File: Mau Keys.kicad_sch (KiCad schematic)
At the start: 2 parts

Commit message: holaaa
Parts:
- added NNV2: ~, symbol MCC NNV2:NNano_v2
- added Switch10, Switch11, Switch12, Switch13, Switch14, Switch15, Switch16, Switch17, Switch6, Switch7, Switch8, Switch9: ~, Switches:keyswitch_cherrymx_alps_choc12_slots_1u, symbol Switches:Kailh_ChocV2_Switch
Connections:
- net S1_P: now reaches Switch1.1
- net S1_P: now also Switch2.1
- net GND: now reaches Switch1.2
- net GND: now also Switch2.2
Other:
- moved on the sheet: Switch1

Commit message: Initial traces
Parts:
- added NNV2_R1: ~, Microcontroller:nice_nano, symbol MCC NNV2:NNano_v2
- added Switch3, Switch4, Switch5, SwitchR_1, SwitchR_10, SwitchR_11, SwitchR_12, SwitchR_13, SwitchR_14, SwitchR_15, SwitchR_16, SwitchR_17, SwitchR_2, SwitchR_3, SwitchR_4, SwitchR_5, SwitchR_6, SwitchR_7, SwitchR_8, SwitchR_9: ~, Switches:keyswitch_cherrymx_alps_choc12_slots_1u, symbol Switches:Kailh_ChocV2_Switch
- NNV2: footprint (none) -> Microcontroller:nice_nano
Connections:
- net GND: now also NNV2.1, NNV2.16, NNV2.4, NNV2.5, Switch10.2, Switch11.2, Switch12.2, Switch13.2, Switch14.2, Switch15.2, Switch16.2, Switch17.2, Switch6.2, Switch7.2, Switch8.2, Switch9.2, NNV2_R1.1, NNV2_R1.16, NNV2_R1.4, NNV2_R1.5, Switch3.2, Switch4.2, Switch5.2, SwitchR_1.2, SwitchR_10.2, SwitchR_11.2, SwitchR_12.2, SwitchR_13.2, SwitchR_14.2, SwitchR_15.2, SwitchR_16.2, SwitchR_17.2, SwitchR_2.2, SwitchR_3.2, SwitchR_4.2, SwitchR_5.2, SwitchR_6.2, SwitchR_7.2, SwitchR_8.2, SwitchR_9.2
- net S9: now reaches Switch9.1
- net S9: now also NNV2.26
- net S12: now reaches Switch12.1
- net S12: now also NNV2.7
- net S15: now reaches Switch15.1
- net S15: now also NNV2.11
- net S11: now reaches Switch11.1
- net S11: now also NNV2.6
- net S13: now reaches Switch13.1
- net S13: now also NNV2.8
- net S17: now reaches Switch17.1
- net S17: now also NNV2.13
- net S10: now reaches Switch10.1
- net S10: now also NNV2.2
- net S16: now reaches Switch16.1
- net S16: now also NNV2.12
- net S1: now reaches NNV2.10
- net S1: now also Switch1.1
- net VBAT: now reaches NNV2.14
- net VBAT: now also NNV2.15, NNV2_R1.14, NNV2_R1.15
- net RESET: now reaches NNV2.17
- net RESET: now also NNV2_R1.17
- net EXT_VCC: now reaches NNV2.18
- net EXT_VCC: now also NNV2_R1.18
- net S5: now reaches NNV2.19
- net S5: now also Switch5.1
- net S4: now reaches NNV2.20
- net S4: now also Switch4.1
- net S3: now reaches NNV2.21
- net S3: now also Switch3.1
- net S2: now reaches NNV2.22
- net S2: now also Switch2.1
- net S6: now reaches NNV2.23
- net S6: now also Switch6.1
- net S7: now reaches NNV2.24
- net S7: now also Switch7.1
- net S8: now reaches NNV2.25
- net S8: now also Switch8.1
- net S14: now reaches NNV2.9
- net S14: now also Switch14.1
- removed net S1_P: Switch1.1, Switch2.1
- new net S10_R: NNV2_R1.2, SwitchR_10.1
- new net S11_R: NNV2_R1.6, SwitchR_11.1
- new net S12_R: NNV2_R1.7, SwitchR_12.1
- new net S13_R: NNV2_R1.8, SwitchR_13.1
- new net S14_R: NNV2_R1.9, SwitchR_14.1
- new net S15_R: NNV2_R1.11, SwitchR_15.1
- new net S16_R: NNV2_R1.12, SwitchR_16.1
- new net S17_R: NNV2_R1.13, SwitchR_17.1
- new net S1_R: NNV2_R1.10, SwitchR_1.1
- new net S2_R: NNV2_R1.22, SwitchR_2.1
- new net S3_R: NNV2_R1.21, SwitchR_3.1
- new net S4_R: NNV2_R1.20, SwitchR_4.1
- new net S5_R: NNV2_R1.19, SwitchR_5.1
- new net S6_R: NNV2_R1.23, SwitchR_6.1
- new net S7_R: NNV2_R1.24, SwitchR_7.1
- new net S8_R: NNV2_R1.25, SwitchR_8.1
- new net S9_R: NNV2_R1.26, SwitchR_9.1
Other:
- moved on the sheet: Switch1

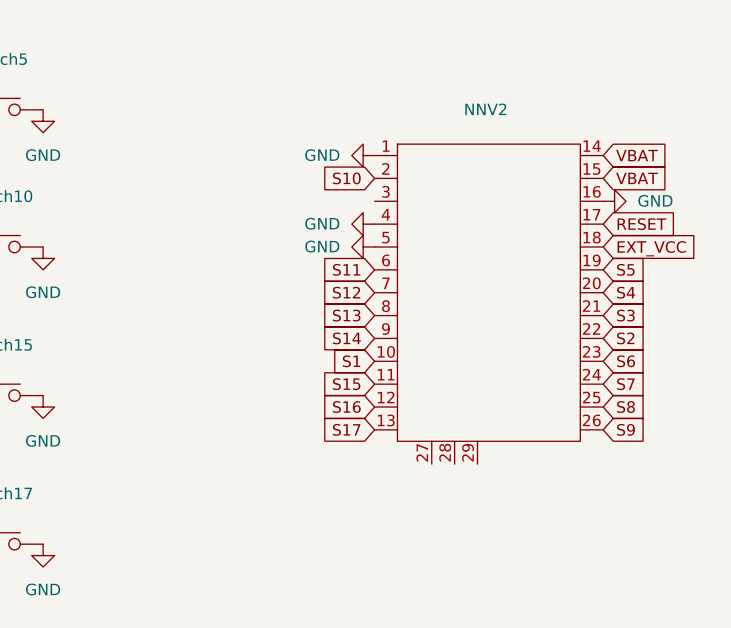
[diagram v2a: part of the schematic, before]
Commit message: Add traces upper left
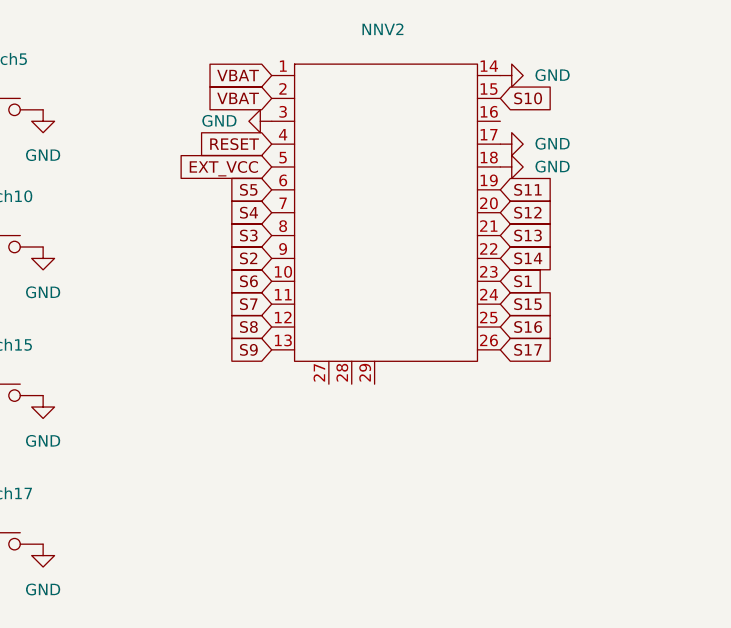
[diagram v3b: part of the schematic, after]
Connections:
- net EXT_VCC: now also NNV2.5; no longer NNV2.18
- net GND: now also NNV2.14, NNV2.17, NNV2.18, NNV2.3; no longer NNV2.1, NNV2.16, NNV2.4, NNV2.5
- net RESET: now also NNV2.4; no longer NNV2.17
- net S1: now also NNV2.23; no longer NNV2.10
- net S10: now also NNV2.15; no longer NNV2.2
- net S11: now also NNV2.19; no longer NNV2.6
- net S12: now also NNV2.20; no longer NNV2.7
- net S13: now also NNV2.21; no longer NNV2.8
- net S14: now also NNV2.22; no longer NNV2.9
- net S15: now also NNV2.24; no longer NNV2.11
- net S16: now also NNV2.25; no longer NNV2.12
- net S17: now also NNV2.26; no longer NNV2.13
- net S2: now also NNV2.9; no longer NNV2.22
- net S3: now also NNV2.8; no longer NNV2.21
- net S4: now also NNV2.7; no longer NNV2.20
- net S5: now also NNV2.6; no longer NNV2.19
- net S6: now also NNV2.10; no longer NNV2.23
- net S7: now also NNV2.11; no longer NNV2.24
- net S8: now also NNV2.12; no longer NNV2.25
- net S9: now also NNV2.13; no longer NNV2.26
- net VBAT: now also NNV2.1, NNV2.2; no longer NNV2.14, NNV2.15
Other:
- moved on the sheet: NNV2

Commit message: Traces upper left
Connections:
- net EXT_VCC: now also NNV2.18; no longer NNV2.5
- net GND: now also NNV2.1, NNV2.16, NNV2.4, NNV2.5; no longer NNV2.14, NNV2.17, NNV2.18, NNV2.3
- net RESET: now also NNV2.17; no longer NNV2.4
- net S1: now also NNV2.2; no longer NNV2.23
- net S10: now also NNV2.13; no longer NNV2.15
- net S10_R: now also NNV2_R1.26; no longer NNV2_R1.2
- net S15: now also NNV2.23; no longer NNV2.24
- net S15_R: now also NNV2_R1.10; no longer NNV2_R1.11
- net S16: now also NNV2.24; no longer NNV2.25
- net S16_R: now also NNV2_R1.11; no longer NNV2_R1.12
- net S17: now also NNV2.25; no longer NNV2.26
- net S17_R: now also NNV2_R1.12; no longer NNV2_R1.13
- net S1_R: now also NNV2_R1.19; no longer NNV2_R1.10
- net S2: now also NNV2.3; no longer NNV2.9
- net S2_R: now also NNV2_R1.20; no longer NNV2_R1.22
- net S3: now also NNV2.6; no longer NNV2.8
- net S4_R: now also NNV2_R1.22; no longer NNV2_R1.20
- net S5: now also NNV2.8; no longer NNV2.6
- net S5_R: now also NNV2_R1.23; no longer NNV2_R1.19
- net S6: now also NNV2.9; no longer NNV2.10
- net S6_R: now also NNV2_R1.24; no longer NNV2_R1.23
- net S7: now also NNV2.10; no longer NNV2.11
- net S7_R: now also NNV2_R1.2; no longer NNV2_R1.24
- net S8: now also NNV2.11; no longer NNV2.12
- net S9: now also NNV2.12; no longer NNV2.13
- net S9_R: now also NNV2_R1.3; no longer NNV2_R1.26
- net VBAT: now also NNV2.14, NNV2.15; no longer NNV2.1, NNV2.2
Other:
- moved on the sheet: NNV2, NNV2_R1

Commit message: finished left
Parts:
- added RSW1, RSW2: SW_Push, reset:SW_RESET, symbol Switch:SW_Push
- added SW_POWER1, SW_POWER2: SW_SPDT, switch_button:smt-slider-switch, symbol Switch:SW_SPDT
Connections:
- net GND: now also RSW1.1, RSW2.1
- net RESET: now also RSW1.2, RSW2.2
- net VBAT: now also SW_POWER1.3 (C), SW_POWER2.3 (C)
- new net BAT+: SW_POWER1.2 (B), SW_POWER2.2 (B)
- no-connect marks 0 -> 2

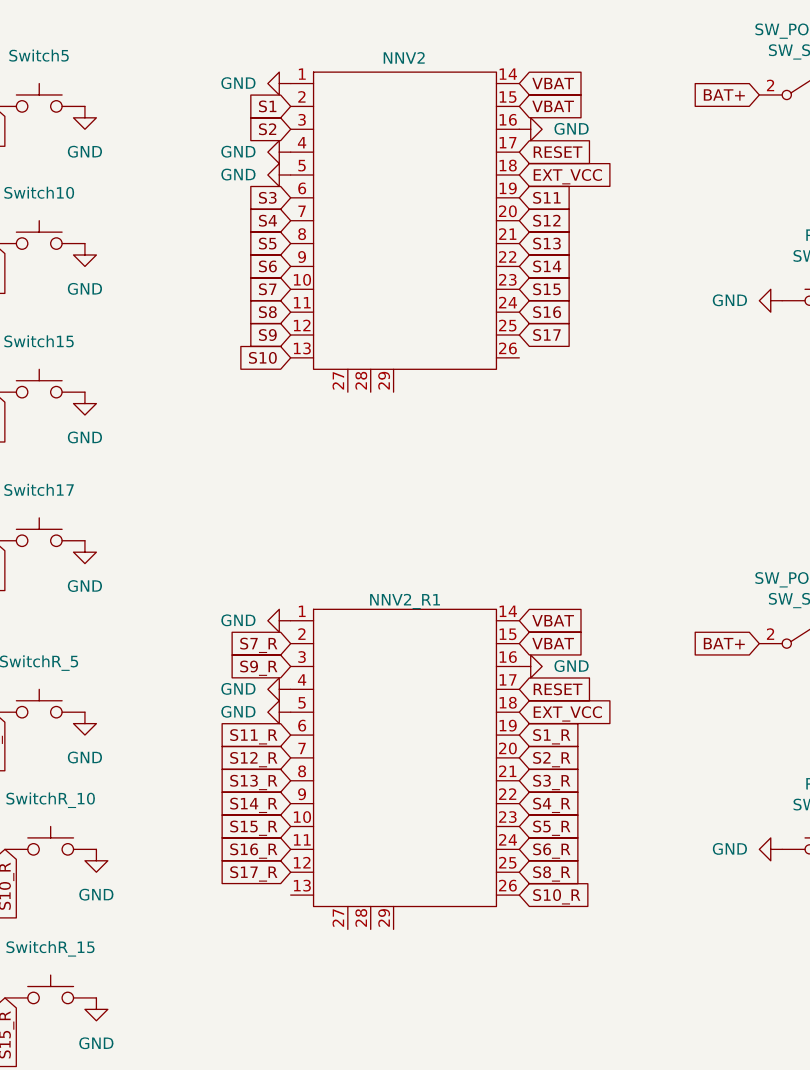
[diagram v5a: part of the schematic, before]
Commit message: fix switch fp
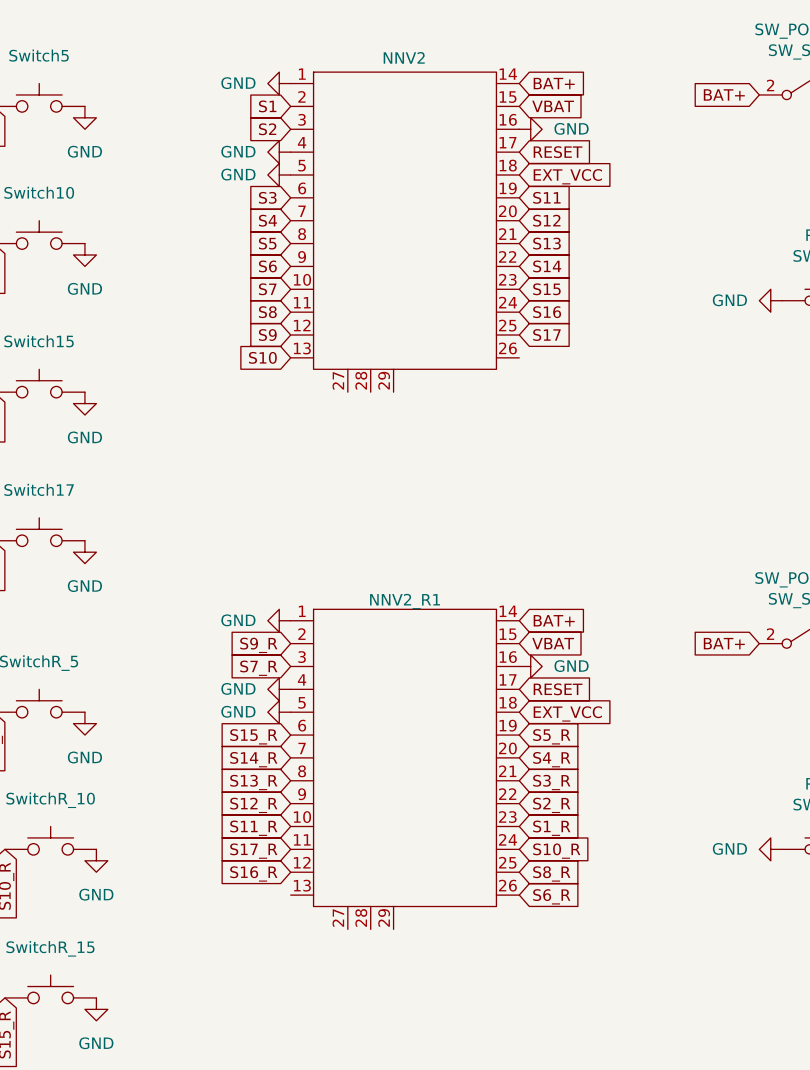
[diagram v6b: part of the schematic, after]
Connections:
- net BAT+: now also NNV2.14, NNV2_R1.14
- net S10_R: now also NNV2_R1.24; no longer NNV2_R1.26
- net S11_R: now also NNV2_R1.10; no longer NNV2_R1.6
- net S12_R: now also NNV2_R1.9; no longer NNV2_R1.7
- net S14_R: now also NNV2_R1.7; no longer NNV2_R1.9
- net S15_R: now also NNV2_R1.6; no longer NNV2_R1.10
- net S16_R: now also NNV2_R1.12; no longer NNV2_R1.11
- net S17_R: now also NNV2_R1.11; no longer NNV2_R1.12
- net S1_R: now also NNV2_R1.23; no longer NNV2_R1.19
- net S2_R: now also NNV2_R1.22; no longer NNV2_R1.20
- net S4_R: now also NNV2_R1.20; no longer NNV2_R1.22
- net S5_R: now also NNV2_R1.19; no longer NNV2_R1.23
- net S6_R: now also NNV2_R1.26; no longer NNV2_R1.24
- net S7_R: now also NNV2_R1.3; no longer NNV2_R1.2
- net S9_R: now also NNV2_R1.2; no longer NNV2_R1.3
- net VBAT: no longer NNV2.14, NNV2_R1.14
